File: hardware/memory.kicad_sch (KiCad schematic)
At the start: 12 parts, among them U15 XL9555

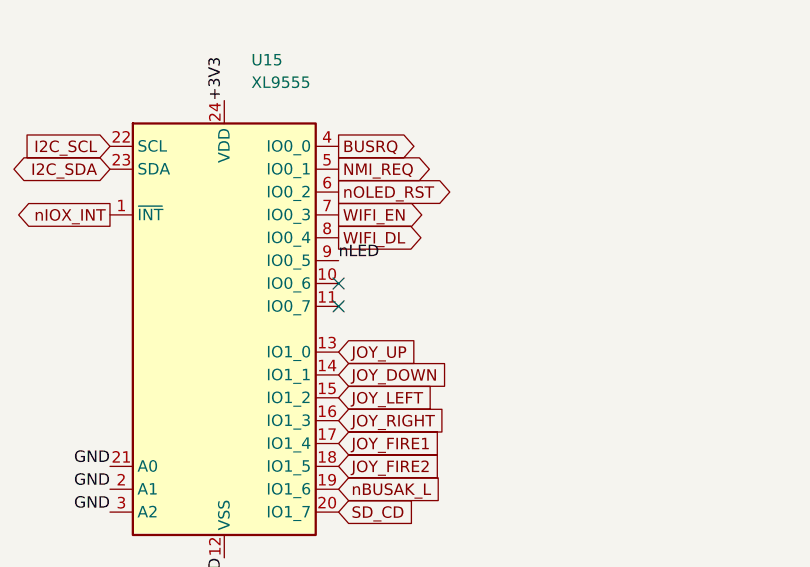
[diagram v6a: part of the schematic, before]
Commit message: v3 prototype 2: bus pull-ups, SD socket power switch, PSRAM footprint
Fixes from proto1 bring-up and issue #21:

- R14 2k2 from nBE (edge A29) to +5V_EDGE. The 74LVC06 only pulls /BE
  low; without a pull-up it rose too slowly and a RAM opcode fetch after
  a served byte read wrong bits. Same value as the bodge on board 1.
- R15-R17 10k pull-ups on GP8-GP10 (nAEN_LO, nAEN_HI, nDATA_OE). The
  RP2350 resets its pads with pull-downs, so in reset and BOOTSEL all
  three buffers were enabled and U1 and U2 both drove MD.
- U32 SY6280AAC current-limited switch on the SD socket's VDD (+3V3_SD),
  enabled from XL9555 P0.6 (SD_PWR_EN), held off by R43 until the
  firmware sets it; R42 15k sets 0.45 A. A card that latches up hits the
  limit instead of pulling +3V3 down and resetting the RP2350B, and a
  wedged card can be power-cycled. R34-R37 move to +3V3_SD so they cannot
  power a switched-off card; the detect pull-up R38 stays on +3V3.
  Firmware: power on after the detect switch reads a card and before any
  SPI; release the SD pins before powering off.
- U22 footprint SOIC-8 3.9 x 4.9 mm. The APS6404L-3SQR-SN is SOP-8
  150 mil (AP Memory package code SN); proto1 had the 208 mil footprint.
  Still DNP; ESP-PSRAM64H (Adafruit 4677) fits the same pads by hand.

Routed by flow.py on the first attempt, DRC clean at every severity
(2119 segments, 385 vias). ERC: the one pre-existing U4 warning only.
$14.90/board at 10 with fees. PSRAM options surveyed in
docs/bom-cost-optimization.md.

Co-Authored-By: Claude Opus 5.5 <noreply@anthropic.com>
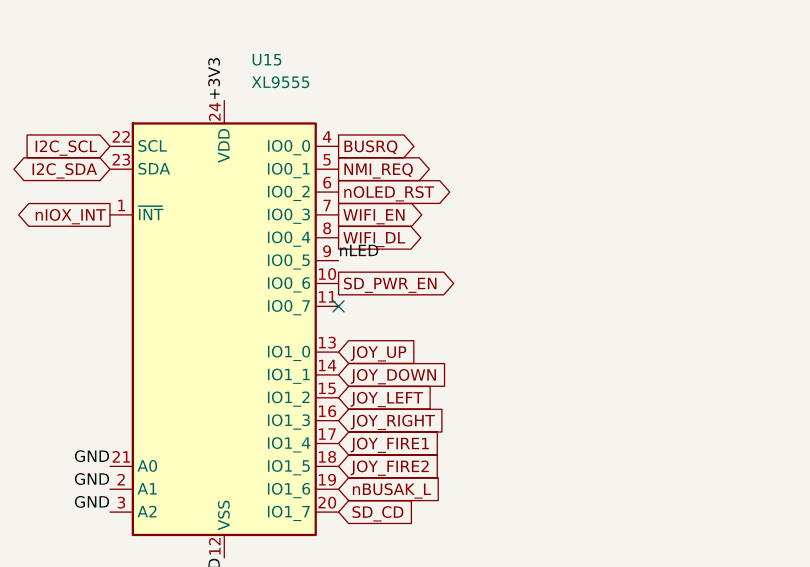
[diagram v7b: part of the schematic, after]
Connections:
- net SD_PWR_EN: now reaches U15.10 (IO0_6)
- no-connect marks 2 -> 1
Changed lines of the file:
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@@
   (global_label "WIFI_DL" (shape output) (at 162.56 100.33 0) (effects (font (size 1.27 1.27)) (justify left)))
   (label "nLED" (at 162.56 102.87 0) (effects (font (size 1.27 1.27)) (justify left bottom)))
-  (no_connect (at 162.56 105.41))
+  (global_label "SD_PWR_EN" (shape output) (at 162.56 105.41 0) (effects (font (size 1.27 1.27)) (justify left)))
   (no_connect (at 162.56 107.95))
   (global_label "JOY_UP" (shape input) (at 162.56 113.03 0) (effects (font (size 1.27 1.27)) (justify left)))

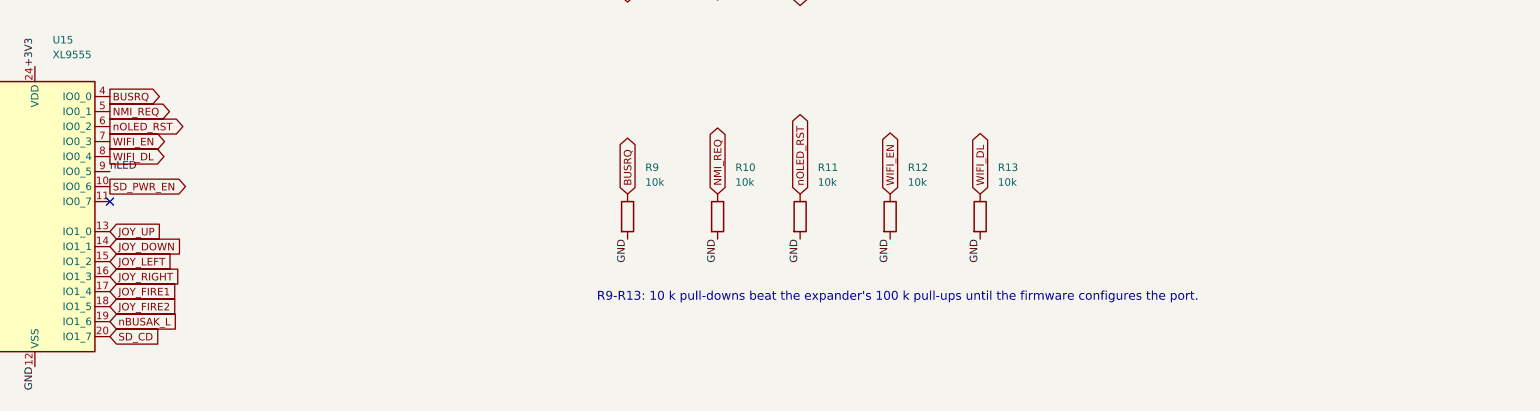
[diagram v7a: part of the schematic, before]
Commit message: v3 proto3: male DE-9, I2C OLED header, buttons in a 2x2 block
- J5: male DE-9 (CONNFLY DS1037-09MNAKT74-0CC, C75750). Atari sticks end
  in a female plug; proto1/2's female footprint mirrors every pin under a
  male part, putting the stick's ground on pin 7 (JOY_5V, open), so nothing
  read. Same body position and mounting holes as proto2.
- J3: 1x4 header for a 1.54in 128x64 SSD1309 I2C module (1 GND, 2 +3V3,
  3 SCL GP43, 4 SDA GP42) on I2C1, R44/R45 4k7 pull-ups. Replaces the 7-pin
  SSD1351 SPI header; GP34, GP41 and expander P0.2 (with R11) are freed.
- SW3 under SW1, SW4 under SW2, so the module covers no buttons; D4/R5
  move left of the ESP32, between H1 and the USB-C socket.

Routed by flow.py on the first attempt: DRC clean at every severity,
2125 segments, 373 vias. ERC: the one existing U4 warning.

Co-Authored-By: Claude Opus 5.5 <noreply@anthropic.com>
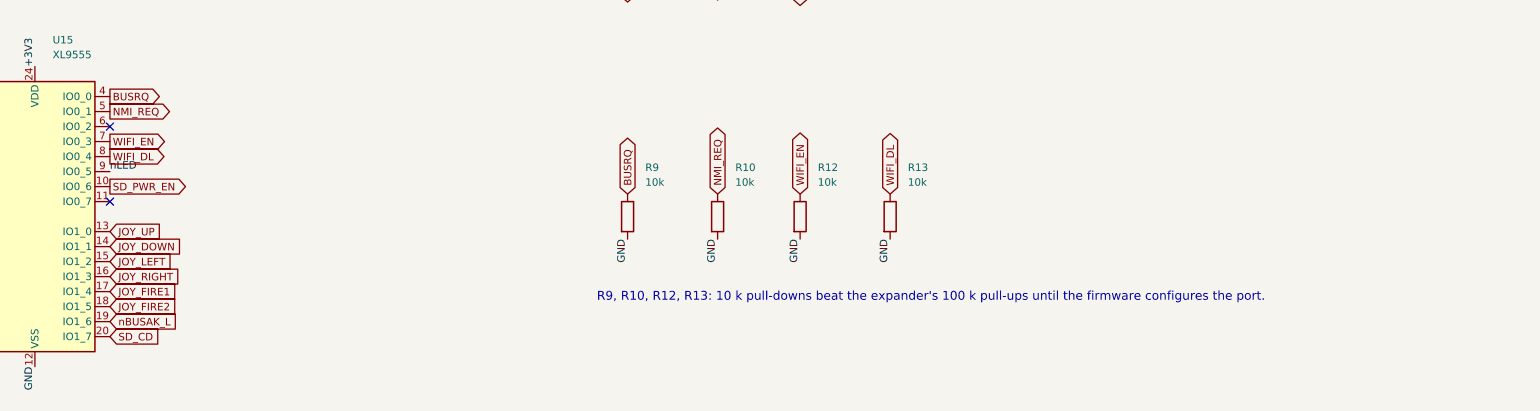
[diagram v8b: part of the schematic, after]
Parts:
- removed R11: 10k, Resistor_SMD:R_0603_1608Metric, symbol Device:R
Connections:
- net nOLED_RST: no longer names the net of U15.6 (IO0_2)
- no-connect marks 1 -> 2
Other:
- note added: "R9, R10, R12, R13: 10 k pull-downs beat the expander's 100 k pull-ups until the firmware configures the port."
- note removed: "R9-R13: 10 k pull-downs beat the expander's 100 k pull-ups until the firmware configures the port."
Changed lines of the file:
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@@
   (global_label "BUSRQ" (shape output) (at 162.56 90.17 0) (effects (font (size 1.27 1.27)) (justify left)))
   (global_label "NMI_REQ" (shape output) (at 162.56 92.71 0) (effects (font (size 1.27 1.27)) (justify left)))
-  (global_label "nOLED_RST" (shape output) (at 162.56 95.25 0) (effects (font (size 1.27 1.27)) (justify left)))
+  (no_connect (at 162.56 95.25))
   (global_label "WIFI_EN" (shape output) (at 162.56 97.79 0) (effects (font (size 1.27 1.27)) (justify left)))
   (global_label "WIFI_DL" (shape output) (at 162.56 100.33 0) (effects (font (size 1.27 1.27)) (justify left)))
@@
   (symbol (lib_id "Device:R") (at 279.4 110.49 0) (unit 1)
     (exclude_from_sim no) (in_bom yes) (on_board yes) (dnp no)
-    (property "Reference" "R11" (at 282.4 102.18 0) (effects (font (size 1.27 1.27)) (justify left)))
+    (property "Reference" "R12" (at 282.4 102.18 0) (effects (font (size 1.27 1.27)) (justify left)))
     (property "Value" "10k" (at 282.4 104.68 0) (effects (font (size 1.27 1.27)) (justify left)))
     (property "Footprint" "Resistor_SMD:R_0603_1608Metric" (at 279.4 110.49 0) (effects (font (size 1.27 1.27)) (justify left) (hide yes)))
@@
     (pin "1")
     (pin "2")
-    (instances (project "tspico-v3" (path "/9088d141-8624-4d5c-91a9-7a3a7a90b3cc/e99fe9a8-9037-4040-a342-12a0ddc42052" (reference "R11") (unit 1))))
+    (instances (project "tspico-v3" (path "/9088d141-8624-4d5c-91a9-7a3a7a90b3cc/e99fe9a8-9037-4040-a342-12a0ddc42052" (reference "R12") (unit 1))))
   )
-  (global_label "nOLED_RST" (shape bidirectional) (at 279.40 106.68 90) (effects (font (size 1.27 1.27)) (justify left)))
+  (global_label "WIFI_EN" (shape bidirectional) (at 279.40 106.68 90) (effects (font (size 1.27 1.27)) (justify left)))
   (label "GND" (at 279.40 114.30 270) (effects (font (size 1.27 1.27)) (justify right bottom)))
   (symbol (lib_id "Device:R") (at 294.64 110.49 0) (unit 1)
     (exclude_from_sim no) (in_bom yes) (on_board yes) (dnp no)
-    (property "Reference" "R12" (at 297.64 102.18 0) (effects (font (size 1.27 1.27)) (justify left)))
+    (property "Reference" "R13" (at 297.64 102.18 0) (effects (font (size 1.27 1.27)) (justify left)))
     (property "Value" "10k" (at 297.64 104.68 0) (effects (font (size 1.27 1.27)) (justify left)))
     (property "Footprint" "Resistor_SMD:R_0603_1608Metric" (at 294.64 110.49 0) (effects (font (size 1.27 1.27)) (justify left) (hide yes)))
@@
     (pin "1")
     (pin "2")
-    (instances (project "tspico-v3" (path "/9088d141-8624-4d5c-91a9-7a3a7a90b3cc/e99fe9a8-9037-4040-a342-12a0ddc42052" (reference "R12") (unit 1))))
-  )
-  (global_label "WIFI_EN" (shape bidirectional) (at 294.64 106.68 90) (effects (font (size 1.27 1.27)) (justify left)))
-  (label "GND" (at 294.64 114.30 270) (effects (font (size 1.27 1.27)) (justify right bottom)))
-  (symbol (lib_id "Device:R") (at 309.88 110.49 0) (unit 1)
-    (exclude_from_sim no) (in_bom yes) (on_board yes) (dnp no)
-    (property "Reference" "R13" (at 312.88 102.18 0) (effects (font (size 1.27 1.27)) (justify left)))
-    (property "Value" "10k" (at 312.88 104.68 0) (effects (font (size 1.27 1.27)) (justify left)))
-    (property "Footprint" "Resistor_SMD:R_0603_1608Metric" (at 309.88 110.49 0) (effects (font (size 1.27 1.27)) (justify left) (hide yes)))
-    (property "Datasheet" "" (at 309.88 110.49 0) (effects (font (size 1.27 1.27)) (justify left) (hide yes)))
-    (property "Description" "" (at 309.88 110.49 0) (effects (font (size 1.27 1.27)) (justify left) (hide yes)))
-    (property "MPN" "0603WAF1002T5E" (at 309.88 110.49 0) (effects (font (size 1.27 1.27)) (justify left) (hide yes)))
-    (property "LCSC" "C25804" (at 309.88 110.49 0) (effects (font (size 1.27 1.27)) (justify left) (hide yes)))
-    (pin "1")
-    (pin "2")
     (instances (project "tspico-v3" (path "/9088d141-8624-4d5c-91a9-7a3a7a90b3cc/e99fe9a8-9037-4040-a342-12a0ddc42052" (reference "R13") (unit 1))))
   )
-  (global_label "WIFI_DL" (shape bidirectional) (at 309.88 106.68 90) (effects (font (size 1.27 1.27)) (justify left)))
-  (label "GND" (at 309.88 114.30 270) (effects (font (size 1.27 1.27)) (justify right bottom)))
-  (text "R9-R13: 10 k pull-downs beat the expander's 100 k pull-ups until the firmware configures the port." (exclude_from_sim no) (at 245 125 0) (effects (font (size 1.5 1.5)) (justify left bottom)))
+  (global_label "WIFI_DL" (shape bidirectional) (at 294.64 106.68 90) (effects (font (size 1.27 1.27)) (justify left)))
+  (label "GND" (at 294.64 114.30 270) (effects (font (size 1.27 1.27)) (justify right bottom)))
+  (text "R9, R10, R12, R13: 10 k pull-downs beat the expander's 100 k pull-ups until the firmware configures the port." (exclude_from_sim no) (at 245 125 0) (effects (font (size 1.5 1.5)) (justify left bottom)))
   (symbol (lib_id "Device:R") (at 250.19 160.02 0) (unit 1)
     (exclude_from_sim no) (in_bom yes) (on_board yes) (dnp no)
